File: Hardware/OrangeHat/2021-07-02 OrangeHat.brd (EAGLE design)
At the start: 85.1 x 56.2 mm, 57 parts, among them CON1-1 JACK_SMD_3MM5, CON2-1 JACK_SMD_3MM5, IC1-485 SN75176

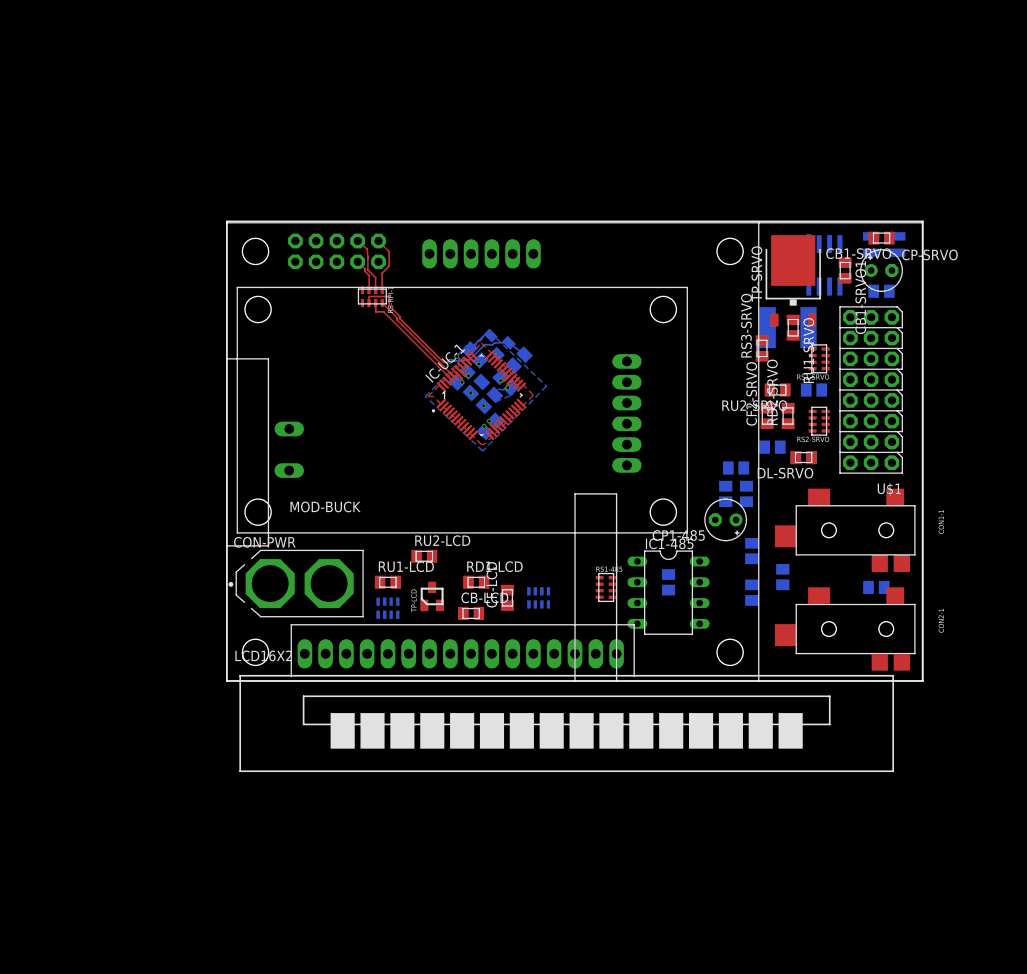
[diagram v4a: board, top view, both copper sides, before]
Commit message: completes initial placement. iterates on routing of power lines.
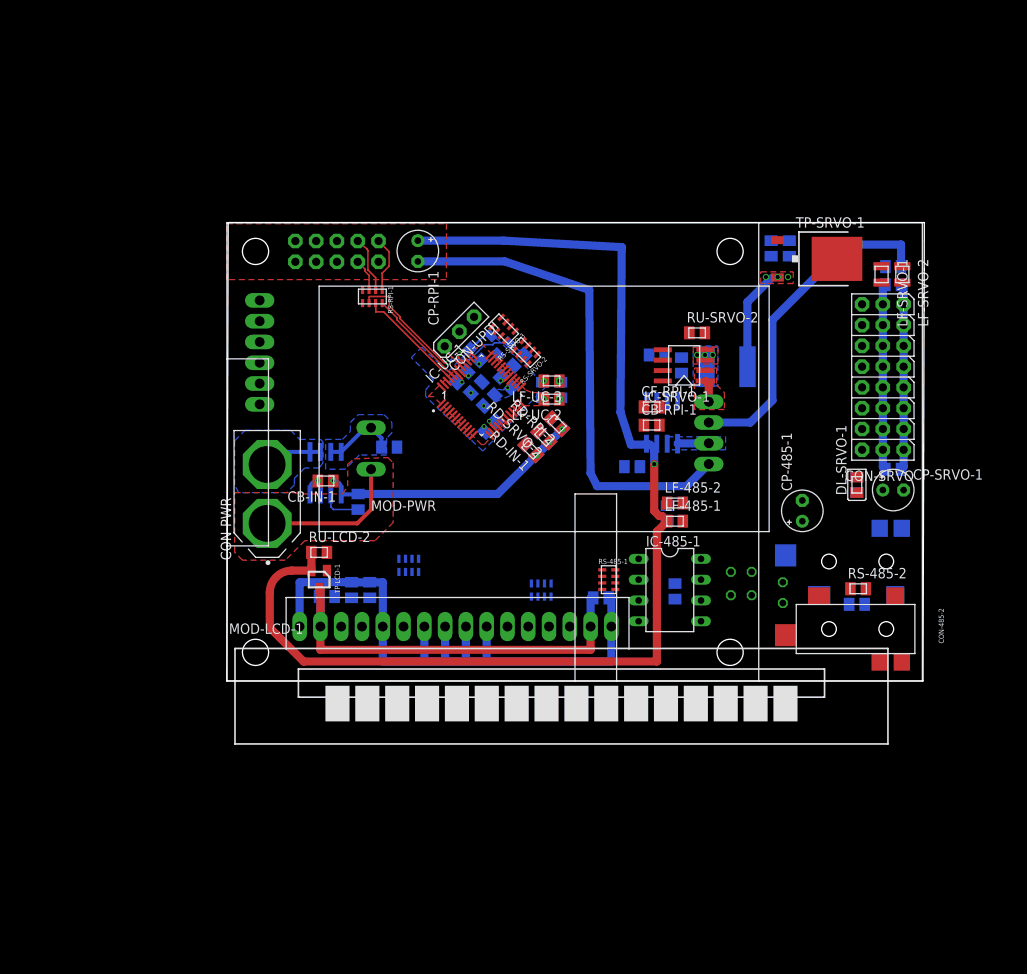
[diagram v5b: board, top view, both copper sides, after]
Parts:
- removed CB-LCD, CB1-485: 100n 50V, 2021-07-02 OrangeHat Library:SMD-M2012
- removed CB1-SRVO, CB1-SRVO1, CB2-SRVO, CB3-SRVO: 1u, 2021-07-02 OrangeHat Library:SMD-M2012
- removed CF-LCD, CF2-SRVO: 10n, 2021-07-02 OrangeHat Library:SMD-M2012
- removed CF1-485: 100n 50v, 2021-07-02 OrangeHat Library:SMD-M2012
- removed CON1-1: JACK_SMD_3MM5, 2021-07-02 OrangeHat Library:JACK_SMD_3MM5
- removed CP-SRVO, CP1-485: 100uF 6V3, 2021-07-02 OrangeHat Library:E2,5-5
- removed DL-SRVO: LED, 2021-07-02 OrangeHat Library:SMD-M2012-POL
- removed F-SRVO: PTC-M5040, 2021-07-02 OrangeHat Library:SMD-M5040
- removed IC-SRVO: ACS712, 2021-07-02 OrangeHat Library:SO8
- removed IC1-485: SN75176, 2021-07-02 OrangeHat Library:DIL08
- removed IMU1: WAVESHARE-IMU-10DOF, 2021-07-02 OrangeHat Library:WAVESHARE-IMU-10DOF
- removed LCD16X2: DISPLAY_16X2_90DEG, 2021-07-02 OrangeHat Library:DISPLAY_16X2_90DEG
- removed LF1-1, LF2-1: BEAD 500mA, 2021-07-02 OrangeHat Library:SMD-M2012
- removed LF1-SRVO, LF1-SRVO1: BEAD 3A, 2021-07-02 OrangeHat Library:SMD-M2016
- removed MOD-BUCK: 2020-03-18-BUCK, 2021-07-02 OrangeHat Library:2020-03-18-BUCK
- removed RD-485, RU-485: 720, 2021-07-02 OrangeHat Library:SMD-M2012
- removed RD-SRVO, RS3-SRVO: 1K, 2021-07-02 OrangeHat Library:SMD-M2012
- removed RD1-LCD, RD2-SRVO: 1k, 2021-07-02 OrangeHat Library:SMD-M2012
- removed RS1-485, RS1-LCD, RS1-SRVO, RS2-LCD, RS2-SRVO: 4X 1K, 2021-07-02 OrangeHat Library:RAC1206
- removed RS2-485, RS3-485: 10, 2021-07-02 OrangeHat Library:SMD-M2012
- removed RT-485: 120, 2021-07-02 OrangeHat Library:SMD-M2012
- removed RU1-LCD, RU2-LCD, RU2-SRVO: 8.2k, 2021-07-02 OrangeHat Library:SMD-M2012
- removed RU1-SRVO: 100k, 2021-07-02 OrangeHat Library:SMD-M2012
- removed TP-LCD: MOS-P-SOT23, 2021-07-02 OrangeHat Library:SOT23
- removed TP-SRVO: MOS-P-TO252, 2021-07-02 OrangeHat Library:TO252
- removed U$1: SERVO8, 2021-07-02 OrangeHat Library:SERVO8
- added CB-485-1: 100n 50v, 2021-07-02 OrangeHat Library:SMD-M2012
- added CB-485-2, CB-LCD-1, CB-UC-5, CB-UC-6: 100n 50V, 2021-07-02 OrangeHat Library:SMD-M2012
- added CB-IN-1, CB-RPI-1, CB-SRVO-1, CB-SRVO-2, CB-SRVO-3, CB-SRVO-4, CF-IN-2, CF-RPI-1, CF-SRVO-1: 1u, 2021-07-02 OrangeHat Library:SMD-M2012
- added CF-IN-1, CF-LCD-1, CF-RPI-2, CF-SRVO-2: 10n, 2021-07-02 OrangeHat Library:SMD-M2012
- added CON-485-1: JACK_SMD_3MM5, 2021-07-02 OrangeHat Library:JACK_SMD_3MM5
- added CON-SRVO: SERVO8-D, 2021-07-02 OrangeHat Library:SERVO8#
- added CON-UPDI: (no value), 2021-07-02 OrangeHat Library:1X03
- added CP-485-1, CP-RPI-1, CP-SRVO-1: 100uF 6V3, 2021-07-02 OrangeHat Library:E2,5-5
- added DL-SRVO-1: LED, 2021-07-02 OrangeHat Library:SMD-M2012-POL
- added F-SRVO-1: PTC-M5040, 2021-07-02 OrangeHat Library:SMD-M5040
- added IC-485-1: SN75176, 2021-07-02 OrangeHat Library:DIL08
- added IC-IN-1, IC-RPI-1, IC-SRVO-1: ACS712, 2021-07-02 OrangeHat Library:SO8
- added LF-485-1, LF-485-2, LF-UC-2, LF-UC-3: BEAD 500mA, 2021-07-02 OrangeHat Library:SMD-M2012
- added LF-SRVO-1, LF-SRVO-2: BEAD 3A, 2021-07-02 OrangeHat Library:SMD-M2016
- added MOD-IMU-1: WAVESHARE-IMU-10DOF, 2021-07-02 OrangeHat Library:WAVESHARE-IMU-10DOF
- added MOD-LCD-1: DISPLAY_16X2_90DEG, 2021-07-02 OrangeHat Library:DISPLAY_16X2_90DEG
- added MOD-PWR: 2020-03-18-BUCK-N5-NHN5, 2021-07-02 OrangeHat Library:2020-03-18-BUCK-NHN5
- added RD-485-1, RU-485-1: 720, 2021-07-02 OrangeHat Library:0207/2V
- added RD-IN-1, RD-LCD-1, RD-RPI-2, RD-SRVO-2: 1k, 2021-07-02 OrangeHat Library:SMD-M2012
- added RD-SRVO-1, RS-SRVO-1: 1K, 2021-07-02 OrangeHat Library:SMD-M2012
- added RS-485-1, RS-LCD-1, RS-LCD-2, RS-SRVO-2, RS-SRVO-3: 4X 1K, 2021-07-02 OrangeHat Library:RAC1206
- added RS-485-2, RS-485-3: 10, 2021-07-02 OrangeHat Library:SMD-M2012
- added RT-485-1: 120, 2021-07-02 OrangeHat Library:0207/2V
- added RU-IN-1, RU-LCD-1, RU-LCD-2, RU-RPI-2, RU-SRVO-2: 8.2k, 2021-07-02 OrangeHat Library:SMD-M2012
- added RU-SRVO-1: 100k, 2021-07-02 OrangeHat Library:SMD-M2012
- added TP-LCD-1: MOS-P-SOT23, 2021-07-02 OrangeHat Library:SOT23
- added TP-SRVO-1: MOS-P-TO252, 2021-07-02 OrangeHat Library:TO252
- moved CON-PWR 11.7 mm to (4.92, 22.9), turned to 90 degrees
- renumbered CON2-1 to CON-485-2
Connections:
- net UC-RST renamed RPI-UC-RST
- removed net N$15: CB1-SRVO.1, LF1-SRVO1.1
- removed net N$3: F-SRVO.1
- removed net N$43: IC-UC-1.25
- removed net VSRVO#A: IC-SRVO.1, IC-SRVO.2, RU2-SRVO.2, TP-SRVO.3
- removed net VSRVO#B: CB1-SRVO.2, IC-SRVO.3, IC-SRVO.4, LF1-SRVO.1
- new net N$1: CF-RPI-1.2, IC-RPI-1.6
- new net N$2: CF-IN-2.2, IC-IN-1.6
- new net UC-IIN: IC-IN-1.7, IC-UC-1.21
- new net VIN#: IC-IN-1.3, IC-IN-1.4, MOD-PWR.VIN+, RU-IN-1.2
- new net VRPI#A: IC-RPI-1.1, IC-RPI-1.2, MOD-PWR.V5.2+
- new net VSRVO#A+: IC-SRVO-1.1, IC-SRVO-1.2, MOD-PWR.V5.8+
- new net VSRVO#A-: CB-SRVO-2.1, LF-SRVO-2.1, MOD-PWR.V5.8-
- new net VSRVO#B+: F-SRVO-1.1, IC-SRVO-1.3, IC-SRVO-1.4, RU-SRVO-2.2
- new net VSRVO#C+: CB-SRVO-2.2, LF-SRVO-1.1, TP-SRVO-1.3
- net CHA485: now also CON-485-1.L, CON-485-1.LX, IC-485-1.6, RD-485-1.2, RT-485-1.1; no longer CON1-1.L, CON1-1.LX, IC1-485.6, RD-485.2, RT-485.1
- net CHB485: now also CON-485-1.R, CON-485-1.RX, IC-485-1.7, RT-485-1.2, RU-485-1.1; no longer CON1-1.R, CON1-1.RX, IC1-485.7, RT-485.2, RU-485.1
- net LCD-PMOS-G: now also RS-LCD-1.1B, RU-LCD-2.2, TP-LCD-1.1; no longer RS1-LCD.1B, RU2-LCD.2, TP-LCD.1
- net N$10: now also MOD-LCD-1.11, RS-LCD-2.1B; no longer LCD16X2.11, RS2-LCD.1B
- net N$11: now also MOD-LCD-1.12, RS-LCD-2.2B; no longer LCD16X2.12, RS2-LCD.2B
- net N$12: now also MOD-LCD-1.13, RS-LCD-2.3B; no longer LCD16X2.13, RS2-LCD.3B
- net N$13: now also MOD-LCD-1.14, RS-LCD-2.4B; no longer LCD16X2.14, RS2-LCD.4B
- net N$19: now also IC-485-1.1, RS-485-1.1B; no longer CF1-485.1, IC1-485.1, LF2-1.1, RS1-485.1B
- net N$20: now also IC-485-1.2, RS-485-1.2B; no longer CF1-485.2, IC1-485.2, LF1-1.1, RS1-485.2B
- net N$21: now also CF-SRVO-1.2, IC-SRVO-1.6; no longer CB1-SRVO1.2, IC-SRVO.6
- net N$22: now also DL-SRVO-1.+, RD-SRVO-1.2; no longer DL-SRVO.+, RD-SRVO.2
- net N$23: now also CON-SRVO.8, RS-SRVO-3.4A; no longer RS2-SRVO.1A, U$1.8
- net N$24: now also CON-SRVO.7, RS-SRVO-3.3A; no longer RS2-SRVO.2A, U$1.7
- net N$25: now also CON-SRVO.6, RS-SRVO-3.2A; no longer RS2-SRVO.3A, U$1.6
- net N$26: now also CON-SRVO.5, RS-SRVO-3.1A; no longer RS2-SRVO.4A, U$1.5
- net N$27: now also CON-SRVO.4, RS-SRVO-2.4A; no longer RS1-SRVO.1A, U$1.4
- net N$28: now also CON-SRVO.3, RS-SRVO-2.3A; no longer RS1-SRVO.2A, U$1.3
- net N$29: now also CON-SRVO.2, RS-SRVO-2.2A; no longer RS1-SRVO.3A, U$1.2
- net N$30: now also CON-SRVO.1, RS-SRVO-2.1A; no longer RS1-SRVO.4A, U$1.1
- net N$44: now also IC-485-1.3, RS-485-1.3B; no longer IC1-485.3, RS1-485.3B
- net N$45: now also IC-485-1.4, RS-485-1.4B; no longer IC1-485.4, RS1-485.4B
- net N$46: now also CON-485-1.SHIELD, RS-485-2.2; no longer CON1-1.SHIELD, RS2-485.2
- net N$47: now also RS-485-3.2; no longer RS3-485.2
- net N$5: now also RS-SRVO-1.2, RU-SRVO-1.2, TP-SRVO-1.1; no longer RS3-SRVO.2, RU1-SRVO.2, TP-SRVO.1
- net N$6: now also F-SRVO-1.2, RU-SRVO-1.1, TP-SRVO-1.2; no longer F-SRVO.2, RU1-SRVO.1, TP-SRVO.2
- net N$7: now also MOD-LCD-1.4, RS-LCD-1.2B; no longer LCD16X2.4, RS1-LCD.2B
- net N$9: now also MOD-LCD-1.6, RS-LCD-1.4B; no longer LCD16X2.6, RS1-LCD.4B
- net UC-485-RXEN#: now also RS-485-1.2A; no longer RS1-485.2A
- net UC-485-RXI: now also RS-485-1.1A; no longer RS1-485.1A
- net UC-485-TXEN: now also RS-485-1.3A; no longer RS1-485.3A
- net UC-485-TXO: now also RS-485-1.4A; no longer RS1-485.4A
- net UC-IMU-FSYNC: now also MOD-IMU-1.FSYNC; no longer IMU1.FSYNC
- net UC-IMU-INT: now also MOD-IMU-1.INT; no longer IMU1.INT
- net UC-IMU-SCL: now also MOD-IMU-1.SCL; no longer IMU1.SCL
- net UC-IMU-SDA: now also MOD-IMU-1.SDA; no longer IMU1.SDA
- net UC-IRPI: now also IC-RPI-1.7, IC-UC-1.25; no longer IC-UC-1.22
- net UC-ISRVO: now also IC-SRVO-1.7, IC-UC-1.23; no longer IC-SRVO.7, IC-UC-1.24
- net UC-LCD-D4: now also RS-LCD-2.1A; no longer RS2-LCD.1A
- net UC-LCD-D5: now also RS-LCD-2.2A; no longer RS2-LCD.2A
- net UC-LCD-D6: now also RS-LCD-2.3A; no longer RS2-LCD.3A
- net UC-LCD-D7: now also RS-LCD-2.4A; no longer RS2-LCD.4A
- net UC-LCD-EN: now also RS-LCD-1.4A; no longer RS1-LCD.4A
- net UC-LCD-PWR#: now also RS-LCD-1.1A; no longer RS1-LCD.1A
- net UC-LCD-RS: now also RS-LCD-1.2A; no longer RS1-LCD.2A
- net UC-SRVO-PWR#: now also RS-SRVO-1.1; no longer RS3-SRVO.1
- net UC-SRVO1: now also RS-SRVO-2.1B; no longer RS1-SRVO.4B
- net UC-SRVO2: now also RS-SRVO-2.2B; no longer RS1-SRVO.3B
- net UC-SRVO3: now also RS-SRVO-2.3B; no longer RS1-SRVO.2B
- net UC-SRVO4: now also RS-SRVO-2.4B; no longer RS1-SRVO.1B
- net UC-SRVO5: now also RS-SRVO-3.1B; no longer RS2-SRVO.4B
- net UC-SRVO6: now also RS-SRVO-3.2B; no longer RS2-SRVO.3B
- net UC-SRVO7: now also RS-SRVO-3.3B; no longer RS2-SRVO.2B
- net UC-SRVO8: now also RS-SRVO-3.4B; no longer RS2-SRVO.1B
- net UC-UPDI: now also CON-UPDI.3
- net UC-VIN: now also CF-IN-1.2, RD-IN-1.2, RU-IN-1.1
- net UC-VRPI: now also CF-RPI-2.2, IC-UC-1.24, RD-RPI-2.2, RU-RPI-2.1; no longer IC-UC-1.21
- net UC-VSRVO: now also CF-SRVO-2.2, IC-UC-1.22, RD-SRVO-2.2, RU-SRVO-2.1; no longer CF2-SRVO.2, IC-UC-1.23, RD2-SRVO.2, RU2-SRVO.1
- net V+485: now also CB-485-2.2, CP-485-1.+, IC-485-1.8, LF-485-1.2, RU-485-1.2; no longer CB1-485.2, CP1-485.+, IC1-485.8, LF1-1.2, RU-485.2
- net V-485: now also CB-485-2.1, CP-485-1.-, IC-485-1.5, LF-485-2.2, RD-485-1.1, RS-485-2.1, RS-485-3.1; no longer CB1-485.1, CP1-485.-, IC1-485.5, LF2-1.2, RD-485.1, RS2-485.1, RS3-485.1
- net VADC+: now also CB-IN-1.2, CB-RPI-1.2, CB-SRVO-1.2, IC-IN-1.8, IC-RPI-1.8, IC-SRVO-1.8
- net VIN+: now also IC-IN-1.1, IC-IN-1.2; no longer MOD-BUCK.VIN+
- net VIN-: now also MOD-PWR.VIN-; no longer MOD-BUCK.VIN-
- net VLCD#: now also CF-LCD-1.2, MOD-LCD-1.3, RD-LCD-1.2, RU-LCD-1.1; no longer CF-LCD.2, LCD16X2.3, RD1-LCD.2, RU1-LCD.1
- net VLCD+: now also CB-LCD-1.2, MOD-LCD-1.15, MOD-LCD-1.2, RU-LCD-1.2, TP-LCD-1.3; no longer CB-LCD.2, LCD16X2.15, LCD16X2.2, RU1-LCD.2, TP-LCD.3
- net VRPI+: now also CB-485-1.2, CB-UC-5.2, CP-RPI-1.+, IC-RPI-1.3, IC-RPI-1.4, LF-485-1.1, LF-UC-2.1, RU-LCD-2.1, RU-RPI-2.2, TP-LCD-1.2; no longer MOD-BUCK.V5.2+
- net VRPI-: now also CB-485-1.1, CB-UC-5.1, CP-RPI-1.-, LF-485-2.1, LF-UC-3.1, MOD-PWR.V5.2-; no longer MOD-BUCK.V5.2-
- net VSRVO+: now also CB-SRVO-3.2, CB-SRVO-4.2, CON-SRVO.1+, CON-SRVO.2+, CON-SRVO.3+, CON-SRVO.4+, CON-SRVO.5+, CON-SRVO.6+, CON-SRVO.7+, CON-SRVO.8+, CP-SRVO-1.+, LF-SRVO-1.2, RD-SRVO-1.1; no longer CB2-SRVO.2, CB3-SRVO.2, CP-SRVO.+, LF1-SRVO.2, MOD-BUCK.V5.8+, RD-SRVO.1, U$1.1+, U$1.2+, U$1.3+, U$1.4+, U$1.5+, U$1.6+, U$1.7+, U$1.8+
- net VSRVO-: now also CB-SRVO-3.1, CB-SRVO-4.1, CON-SRVO.1-, CON-SRVO.2-, CON-SRVO.3-, CON-SRVO.4-, CON-SRVO.5-, CON-SRVO.6-, CON-SRVO.7-, CON-SRVO.8-, CP-SRVO-1.-, DL-SRVO-1.-, LF-SRVO-2.2; no longer CB2-SRVO.1, CB3-SRVO.1, CP-SRVO.-, DL-SRVO.-, LF1-SRVO1.2, MOD-BUCK.V5.8-, U$1.1-, U$1.2-, U$1.3-, U$1.4-, U$1.5-, U$1.6-, U$1.7-, U$1.8-
- net VUC+: now also CB-UC-6.2, CON-UPDI.2, LF-UC-2.2, MOD-IMU-1.VCC; no longer IC-SRVO.8, IMU1.VCC, MOD-BUCK.V5.0+, RU2-LCD.1, TP-LCD.2
- net VUC-: now also CB-IN-1.1, CB-LCD-1.1, CB-RPI-1.1, CB-SRVO-1.1, CB-UC-6.1, CF-IN-1.1, CF-IN-2.1, CF-LCD-1.1, CF-RPI-1.1, CF-RPI-2.1, CF-SRVO-1.1, CF-SRVO-2.1, CON-UPDI.1, IC-IN-1.5, IC-RPI-1.5, IC-SRVO-1.5, LF-UC-3.2, MOD-IMU-1.COM, MOD-LCD-1.1, MOD-LCD-1.10, MOD-LCD-1.16, MOD-LCD-1.5, MOD-LCD-1.7, MOD-LCD-1.8, MOD-LCD-1.9, RD-IN-1.1, RD-LCD-1.1, RD-RPI-2.1, RD-SRVO-2.1; no longer CB-LCD.1, CB1-SRVO1.1, CF-LCD.1, CF2-SRVO.1, IC-SRVO.5, IMU1.COM, LCD16X2.1, LCD16X2.10, LCD16X2.16, LCD16X2.5, LCD16X2.7, LCD16X2.8, LCD16X2.9, MOD-BUCK.V5.0-, RD1-LCD.1, RD2-SRVO.1
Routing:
- net VRPI+: track 0.00 -> 141.6 mm, vias 0 -> 2
- net VUC-: track 4.20 -> 115.3 mm, vias 3 -> 8
- net VRPI-: track 0.00 -> 60.7 mm, vias 0 -> 1
- net VLCD+: track 0.00 -> 51.0 mm
- net VSRVO#A-: track 0.00 -> 41.0 mm
- net VSRVO-: track 0.00 -> 23.0 mm
- net VSRVO+: track 0.00 -> 22.8 mm
- net VIN-: track 0.00 -> 18.3 mm
- net N$6: track 0.00 -> 12.0 mm, vias 0 -> 3
- net VIN#: track 0.00 -> 9.05 mm
- net VIN+: track 0.00 -> 7.15 mm
- net N$2: track 0.00 -> 4.99 mm
- net VRPI#A: track 0.00 -> 3.83 mm
- net UC-UPDI: track 0.00 -> 3.36 mm
- net VSRVO#A+: track 0.00 -> 2.71 mm
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- added copper zone on layer 1, net N$6
- added copper zone on layer 16, net VIN#
- added copper zone on layer 16, net VIN+
- added copper zone on layer 1, net VIN-
- added copper zone on layer 16, net VRPI#A
- added copper zone on layer 1, net VRPI+
- added copper zone on layer 1, net VSRVO#A+
- added copper zone on layer 1, net VSRVO#B+
- added copper zone on layer 16, net VSRVO#B+
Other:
- board size 85.1 x 56.2 mm -> 85.2 x 56 mm

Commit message: routing of power lines. complete autoroute of signals.
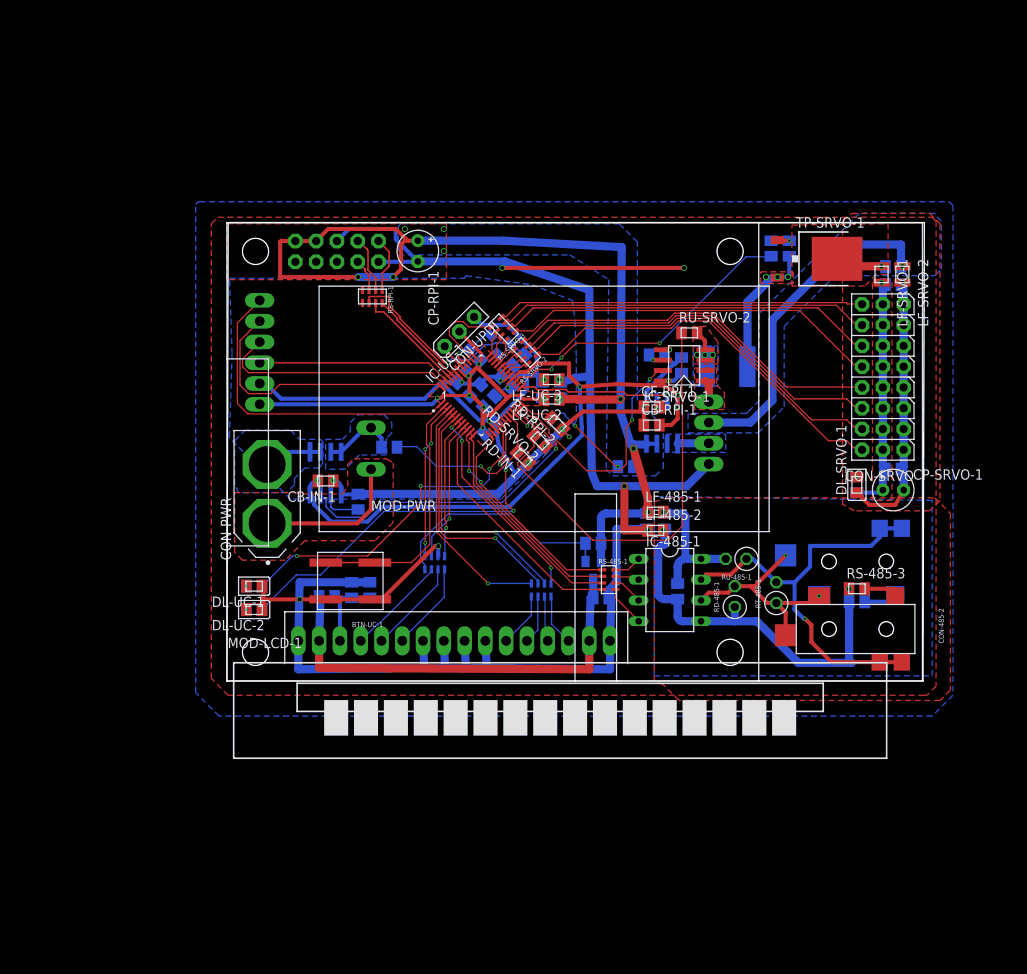
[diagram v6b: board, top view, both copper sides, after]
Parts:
- removed CP-485-1: 100uF 6V3, 2021-07-02 OrangeHat Library:E2,5-5
- added BTN-UC-1: BTN_NO-M8070, 2021-07-02 OrangeHat Library:SMD_BTN_M8070
- added CB-485-3: 1u 50V, 2021-07-02 OrangeHat Library:SMD-M2012
- added DL-UC-1, DL-UC-2: LED, 2021-07-02 OrangeHat Library:SMD-M2012-POL
- added RS-UC-1, RS-UC-2: 330, 2021-07-02 OrangeHat Library:SMD-M2012
- CB-485-2: value 100n 50V -> 100n 50v
- CB-SRVO-2, CB-SRVO-3: value 1u -> 100n
- moved TP-LCD-1 33.5 mm to (44.8, 13.5), flipped to the bottom
- moved RU-LCD-2 33.5 mm to (44.8, 16.8), flipped to the bottom
- moved CB-485-2 8.67 mm to (53.5, 19.5)
- moved LF-485-2 4.10 mm to (52.4, 18.4)
- moved RS-LCD-1 3.19 mm to (25.4, 14.4)
- moved CB-485-1 2.71 mm to (51.3, 19.5), turned to 90 degrees
- moved LF-485-1 2.63 mm to (52.4, 20.6)
- moved RS-485-3 1.90 mm to (77.0, 11.3), flipped to the top, turned to 0 degrees
- moved MOD-LCD-1 1.75 mm to (0.73, -9.32)
- moved RU-485-1 1.71 mm to (62.2, 14.9), flipped to the top, turned to 180 degrees
- moved RS-485-2 1.60 mm to (77.0, 9.68), flipped to the bottom, turned to 180 degrees
- moved CF-IN-1 1.35 mm to (36.2, 27.3)
- moved RD-IN-1 1.35 mm to (36.2, 27.3)
- moved RU-SRVO-2 0.95 mm to (56.5, 42.5)
- moved RD-485-1 0.81 mm to (62.1, 10.3), flipped to the top, turned to 90 degrees
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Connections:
- net N$14 renamed NC-1
- net N$8 renamed NC-2
- removed net N$51: IC-UC-1.17
- removed net N$52: IC-UC-1.16
- removed net N$62: IC-UC-1.2
- removed net V+485: CB-485-2.2, CP-485-1.+, IC-485-1.8, LF-485-1.2, RU-485-1.2
- removed net V-485: CB-485-2.1, CP-485-1.-, IC-485-1.5, LF-485-2.2, RD-485-1.1, RS-485-2.1, RS-485-3.1
- new net N$15: DL-UC-2.+, RS-UC-2.2
- new net N$3: MOD-LCD-1.5, RS-LCD-1.3B
- new net N$4: DL-UC-1.+, RS-UC-1.2
- new net UC-BTN-NO: BTN-UC-1.2B, BTN-UC-1.3B, IC-UC-1.2
- new net UC-LED-1: IC-UC-1.16, RS-UC-1.1
- new net UC-LED-2: IC-UC-1.17, RS-UC-2.1
- new net V485+: CB-485-2.2, CB-485-3.2, IC-485-1.8, LF-485-1.2, RU-485-1.2
- new net V485-: CB-485-2.1, CB-485-3.1, IC-485-1.5, LF-485-2.2, RD-485-1.1, RS-485-2.1, RS-485-3.1
- net VRPI-: now also BTN-UC-1.1A, BTN-UC-1.4A, CB-LCD-1.1, CF-LCD-1.1, DL-UC-1.-, DL-UC-2.-, MOD-LCD-1.1, MOD-LCD-1.10, MOD-LCD-1.16, MOD-LCD-1.7, MOD-LCD-1.8, MOD-LCD-1.9, RD-LCD-1.1, RS-LCD-1.3A
- net VUC-: no longer CB-LCD-1.1, CF-LCD-1.1, MOD-LCD-1.1, MOD-LCD-1.10, MOD-LCD-1.16, MOD-LCD-1.5, MOD-LCD-1.7, MOD-LCD-1.8, MOD-LCD-1.9, RD-LCD-1.1
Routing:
- net VRPI-: track 60.7 -> 234.0 mm, vias 1 -> 7
- net VADC+: track 3.57 -> 82.0 mm, vias 2 -> 6
- net UC-VSRVO: track 0.00 -> 57.2 mm, vias 0 -> 1
- net VUC+: track 3.95 -> 60.5 mm, vias 6 -> 7
- net CHB485: track 0.00 -> 52.0 mm, vias 0 -> 1
- net V485-: track 0.00 -> 49.9 mm, vias 0 -> 2
- net N$30: track 0.00 -> 47.9 mm
- net UC-LED-2: track 0.00 -> 47.7 mm, vias 0 -> 3
- net N$29: track 0.00 -> 47.5 mm
- net N$28: track 0.00 -> 47.0 mm
- net N$27: track 0.00 -> 46.6 mm
- net N$26: track 0.00 -> 46.3 mm
- net N$25: track 0.00 -> 45.8 mm
- net N$24: track 0.00 -> 45.4 mm
- net N$23: track 0.00 -> 44.9 mm
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- added copper zone on layer 1, net V485-
- added copper zone on layer 16, net V485-
- added copper zone on layer 16, net VRPI+
- added copper zone on layer 1, net VRPI-
- added copper zone on layer 16, net VRPI-
- added copper zone on layer 16, net VSRVO#A-
- added copper zone on layer 1, net VSRVO#C+
- added copper zone on layer 1, net VSRVO+
- added copper zone on layer 1, net VSRVO-

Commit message: completes routing. generates gerber files. validates ERC and DRC with eurocircuit
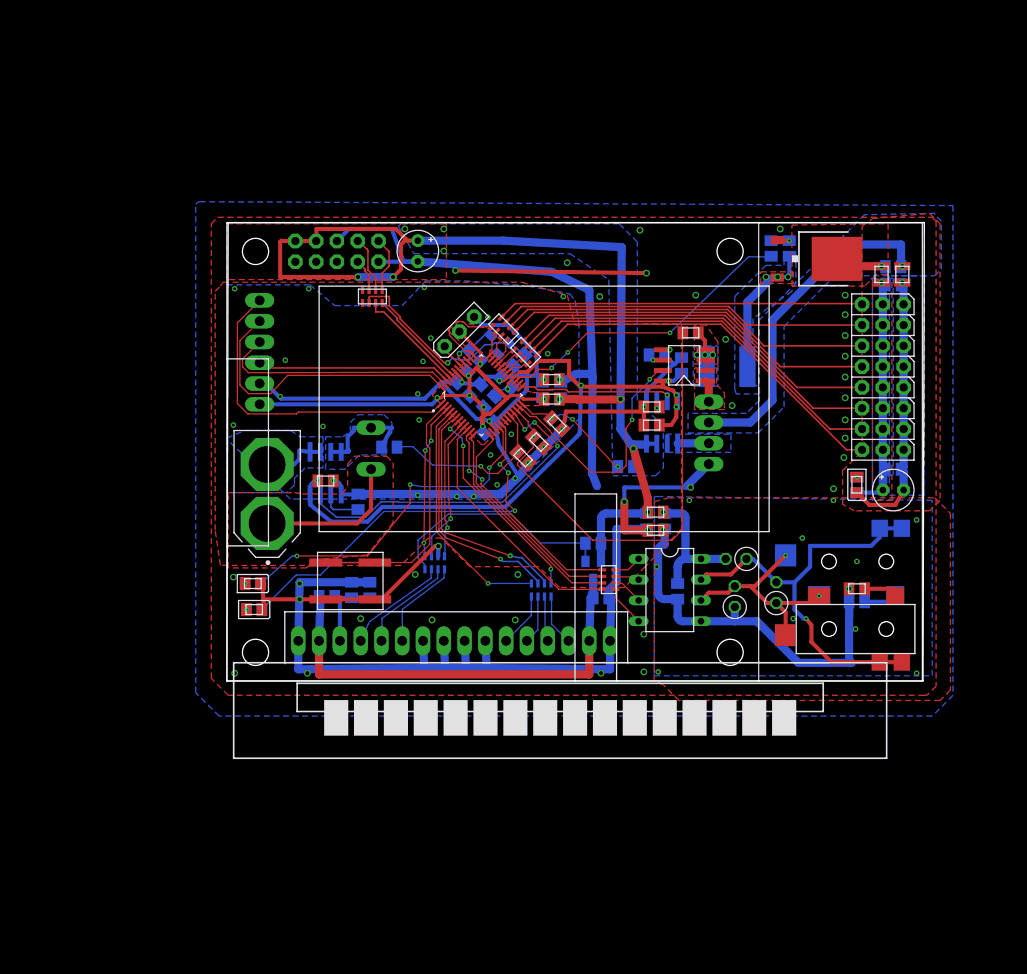
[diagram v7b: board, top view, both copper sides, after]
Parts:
- added U$1: (no value), 2021-07-02 OrangeHat Library:SIGNATURE_ADROBOT_SMALL
- added U$2: (no value), 2021-07-02 OrangeHat Library:SIGNATURE_ORANGEBOT_SMALL
- CB-485-1, CB-485-2: value 100n 50v -> 100n
- CB-485-3: value 1u 50V -> 1u
- CB-IN-1, CB-RPI-1, CB-SRVO-1: value 1u -> 100n
- CB-LCD-1, CB-UC-1, CB-UC-2, CB-UC-3, CB-UC-4, CB-UC-5, CB-UC-6: value 100n 50V -> 100n
- CF-IN-2, CF-RPI-1, CF-SRVO-1: value 1u -> 10n
- CON-UPDI: value (none) -> UPDI
- DL-UC-1: value LED -> GREEN
- DL-UC-2: value LED -> BLUE
- RD-485-1, RT-485-1, RU-485-1: device 2021-07-02 OrangeHat Library:0207/2V -> 2021-07-02 OrangeHat Library:TH-2MM54-V
- RD-RPI-2, RD-SRVO-2: value 1k -> 10k
- RU-RPI-2, RU-SRVO-2: value 8.2k -> 10k
- TN-UC-1: value MOS-N-SOT23 -> 2N7002
- TP-LCD-1: value MOS-P-SOT23 -> BSS84
- TP-SRVO-1: value MOS-P-TO252 -> 4P03L11
- moved DL-UC-1 0.35 mm to (3.17, 11.9)
- moved RS-UC-1 0.35 mm to (3.17, 11.9)
- moved CF-SRVO-2 0.22 mm to (38.1, 29.2)
- moved RD-SRVO-2 0.22 mm to (38.1, 29.2)
- moved RU-SRVO-2 0.16 mm to (56.7, 42.5)
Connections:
- removed net N$17: RS-RPI-1.4A
- removed net N$42: IC-UC-1.26
- removed net N$49: IC-UC-1.19
- removed net N$50: IC-UC-1.18
- removed net N$53: RS-RPI-1.4B
- removed net NC-1: IC-UC-1.38
- removed net NC-2: IC-UC-1.39
- removed net RPI-SCL: CON-RPI.5
- removed net RPI-SDA: CON-RPI.3
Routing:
- net VIN#: track 9.05 -> 12.9 mm
- net VLCD+: track 53.1 -> 54.5 mm
- net VRPI+: track 123.7 -> 124.7 mm
- net UC-IMU-INT: track 34.5 -> 35.5 mm
- net VRPI-: track 234.0 -> 233.2 mm, vias 7 -> 37
- net VIN+: track 7.15 -> 7.84 mm
- net UC-LCD-D6: track 29.9 -> 29.2 mm
- net UC-IIN: track 42.1 -> 42.7 mm
- net N$3: track 11.6 -> 12.2 mm
- net VUC-: track 138.2 -> 137.9 mm, vias 11 -> 31
- net V485-: vias 2 -> 12
- added copper zone on layer 16, net N$6
- added copper zone on layer 16, net VSRVO+
- added copper zone on layer 16, net VSRVO-
- added copper zone on layer 1, net VUC-
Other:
- board text added: "BLUE"
- board text added: "GREEN"
- board text added: "OrangeHat"
- board text added: "Orso Eric 2021-08"
